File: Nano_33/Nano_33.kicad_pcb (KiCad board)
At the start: 2 copper layers, 2 parts, among them J1 Arduino-NANO-33

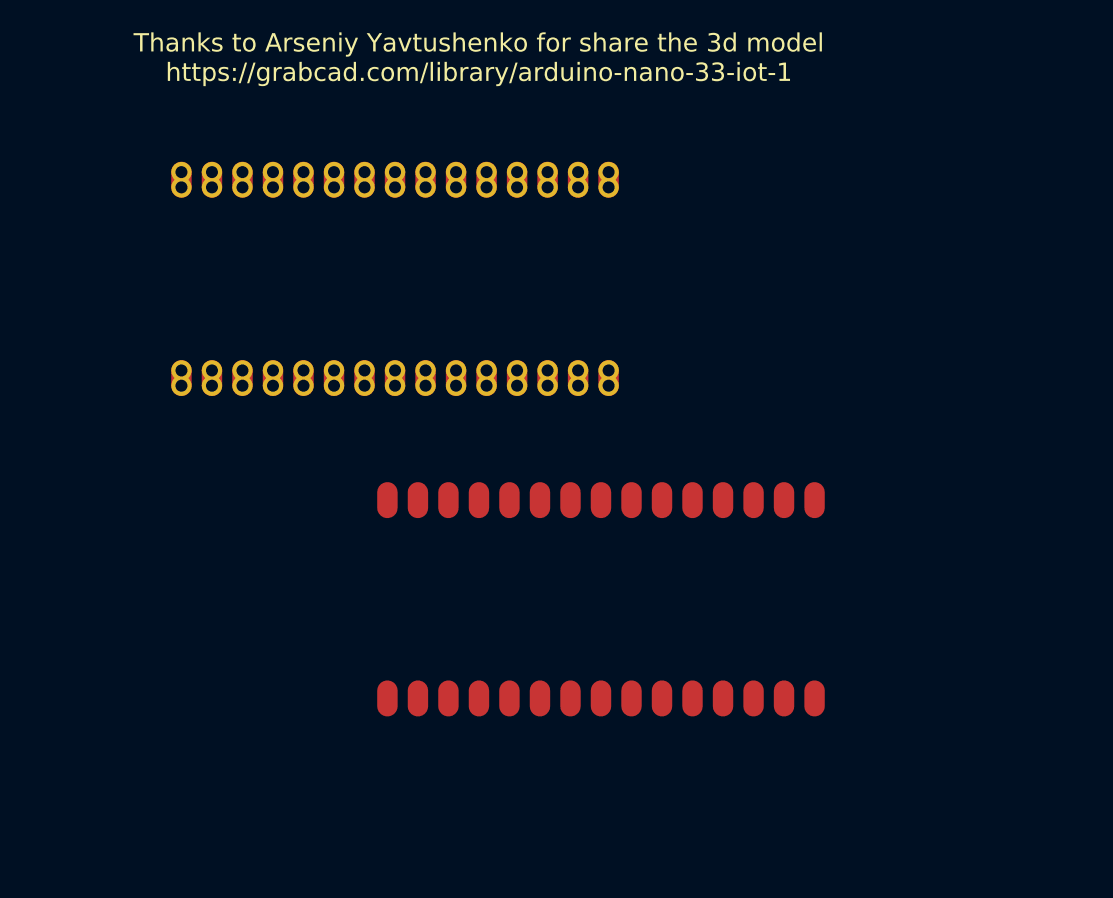
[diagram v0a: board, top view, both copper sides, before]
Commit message: Add No Castell Footprint
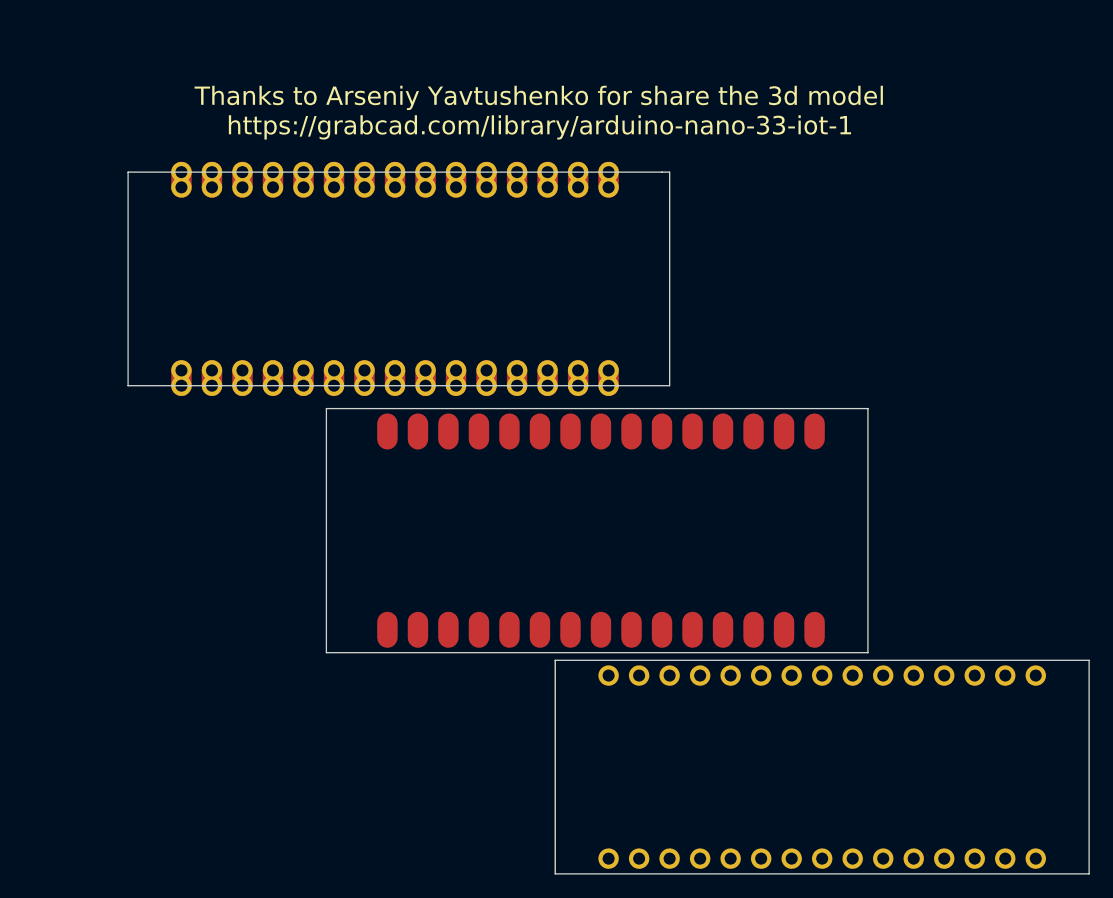
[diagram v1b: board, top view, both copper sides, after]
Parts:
- added REF**: NANO_33_Socket, Arduino:NANO_33_Socket, F.Cu at (186.1, 121.3)
- moved REF** 5.72 mm to (167.6, 101.6)
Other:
- board outline added: 80 x 58.4 mm
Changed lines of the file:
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@@
   (general
     (thickness 1.6002)
-    (drawings 1)
+    (drawings 14)
     (tracks 0)
     (zones 0)
-    (modules 2)
+    (modules 3)
     (nets 29)
   )
@@
     (add_net /VUSB)
   )
-  (module Arduino:NANO_33_Footprint_SMD_Castell (layer Front)
-    (at 167.64 107.315)
+  (module Arduino:NANO_33_Socket (layer Front)
+    (at 186.055 121.285)
     (descr "Through hole straight socket strip, 1x15, 2.54mm pitch")
     (tags "Through hole socket strip THT 1x15 2.54mm single row")
-    (fp_text reference REF** (at 0 -13.335) (layer F.Fab)
-      (effects (font (size 1 1) (thickness 0.15)))
-    )
-    (fp_text value NANO_33_Footprint_SMD_Castell (at 0 12.065) (layer F.Fab)
+    (fp_text reference REF** (at 20.32 -10.16) (layer F.Fab)
+      (effects (font (size 1 1) (thickness 0.15)))
+    )
+    (fp_text value NANO_33_Socket (at 0 12.065) (layer F.Fab)
+      (effects (font (size 1 1) (thickness 0.15)))
+    )
+    (fp_text user %R (at 0 -7.62) (layer F.Fab)
+      (effects (font (size 1 1) (thickness 0.15)))
+    )
+    (fp_line (start -19.05 -8.89) (end 19.05 -8.89) (layer F.Fab) (width 0.1))
+    (fp_line (start -19.05 -6.35) (end -19.05 -8.89) (layer F.Fab) (width 0.1))
+    (fp_line (start 18.415 -6.35) (end -19.05 -6.35) (layer F.Fab) (width 0.1))
+    (fp_line (start 19.05 -6.985) (end 18.415 -6.35) (layer F.Fab) (width 0.1))
+    (fp_line (start 19.05 -8.89) (end 19.05 -6.985) (layer F.Fab) (width 0.1))
+    (fp_line (start -19.05 8.89) (end -19.05 6.985) (layer F.Fab) (width 0.1))
+    (fp_line (start -19.05 6.985) (end -18.415 6.35) (layer F.Fab) (width 0.1))
+    (fp_line (start -18.415 6.35) (end 19.05 6.35) (layer F.Fab) (width 0.1))
+    (fp_line (start 19.05 6.35) (end 19.05 8.89) (layer F.Fab) (width 0.1))
+    (fp_line (start 19.05 8.89) (end -19.05 8.89) (layer F.Fab) (width 0.1))
+    (fp_text user %R (at 0 7.62 180) (layer F.Fab)
+      (effects (font (size 1 1) (thickness 0.15)))
+    )
+    (fp_line (start 22 8.89) (end 22 -8.89) (layer F.Fab) (width 0.12))
+    (fp_line (start -22 8.89) (end 22 8.89) (layer F.Fab) (width 0.12))
+    (fp_line (start -22 8.89) (end -22 -8.89) (layer F.Fab) (width 0.12))
+    (fp_line (start -22 -8.89) (end 22 -8.89) (layer F.Fab) (width 0.12))
+    (fp_poly (pts (xy -22.86 3.175) (xy -18.415 3.175) (xy -18.415 -3.175) (xy -22.86 -3.175)) (layer F.Fab) (width 0.1))
+    (fp_poly (pts (xy -3.175 3.175) (xy 3.175 3.175) (xy 3.175 -3.175) (xy -3.175 -3.175)) (layer F.Fab) (width 0.1))
+    (fp_poly (pts (xy 8.89 4.445) (xy 21.59 4.445) (xy 21.59 -4.445) (xy 8.89 -4.445)) (layer F.Fab) (width 0.1))
+    (pad 30 thru_hole oval (at -17.78 -7.62 270) (size 1.7 1.7) (drill 1) (layers *.Cu *.Mask))
+    (pad 29 thru_hole oval (at -15.24 -7.62 270) (size 1.7 1.7) (drill 1) (layers *.Cu *.Mask))
+    (pad 28 thru_hole oval (at -12.7 -7.62 270) (size 1.7 1.7) (drill 1) (layers *.Cu *.Mask))
+    (pad 27 thru_hole oval (at -10.16 -7.62 270) (size 1.7 1.7) (drill 1) (layers *.Cu *.Mask))
+    (pad 26 thru_hole oval (at -7.62 -7.62 270) (size 1.7 1.7) (drill 1) (layers *.Cu *.Mask))
+    (pad 25 thru_hole oval (at -5.08 -7.62 270) (size 1.7 1.7) (drill 1) (layers *.Cu *.Mask))
+    (pad 24 thru_hole oval (at -2.54 -7.62 270) (size 1.7 1.7) (drill 1) (layers *.Cu *.Mask))
+    (pad 23 thru_hole oval (at 0 -7.62 270) (size 1.7 1.7) (drill 1) (layers *.Cu *.Mask))
+    (pad 22 thru_hole oval (at 2.54 -7.62 270) (size 1.7 1.7) (drill 1) (layers *.Cu *.Mask))
+    (pad 21 thru_hole oval (at 5.08 -7.62 270) (size 1.7 1.7) (drill 1) (layers *.Cu *.Mask))
+    (pad 20 thru_hole oval (at 7.62 -7.62 270) (size 1.7 1.7) (drill 1) (layers *.Cu *.Mask))
+    (pad 19 thru_hole oval (at 10.16 -7.62 270) (size 1.7 1.7) (drill 1) (layers *.Cu *.Mask))
+    (pad 18 thru_hole oval (at 12.7 -7.62 270) (size 1.7 1.7) (drill 1) (layers *.Cu *.Mask))
+    (pad 17 thru_hole oval (at 15.24 -7.62 270) (size 1.7 1.7) (drill 1) (layers *.Cu *.Mask))
+    (pad 16 thru_hole circle (at 17.78 -7.62 270) (size 1.7 1.7) (drill 1) (layers *.Cu *.Mask))
+    (pad 12 thru_hole oval (at 10.16 7.62 90) (size 1.7 1.7) (drill 1) (layers *.Cu *.Mask))
+    (pad 15 thru_hole oval (at 17.78 7.62 90) (size 1.7 1.7) (drill 1) (layers *.Cu *.Mask))
+    (pad 1 thru_hole circle (at -17.78 7.62 90) (size 1.7 1.7) (drill 1) (layers *.Cu *.Mask))
+    (pad 2 thru_hole oval (at -15.24 7.62 90) (size 1.7 1.7) (drill 1) (layers *.Cu *.Mask))
+    (pad 3 thru_hole oval (at -12.7 7.62 90) (size 1.7 1.7) (drill 1) (layers *.Cu *.Mask))
+    (pad 4 thru_hole oval (at -10.16 7.62 90) (size 1.7 1.7) (drill 1) (layers *.Cu *.Mask))
+    (pad 5 thru_hole oval (at -7.62 7.62 90) (size 1.7 1.7) (drill 1) (layers *.Cu *.Mask))
+    (pad 14 thru_hole oval (at 15.24 7.62 90) (size 1.7 1.7) (drill 1) (layers *.Cu *.Mask))
+    (pad 6 thru_hole oval (at -5.08 7.62 90) (size 1.7 1.7) (drill 1) (layers *.Cu *.Mask))
+    (pad 11 thru_hole oval (at 7.62 7.62 90) (size 1.7 1.7) (drill 1) (layers *.Cu *.Mask))
+    (pad 10 thru_hole oval (at 5.08 7.62 90) (size 1.7 1.7) (drill 1) (layers *.Cu *.Mask))
+    (pad 7 thru_hole oval (at -2.54 7.62 90) (size 1.7 1.7) (drill 1) (layers *.Cu *.Mask))
+    (pad 8 thru_hole oval (at 0 7.62 90) (size 1.7 1.7) (drill 1) (layers *.Cu *.Mask))
+    (pad 9 thru_hole oval (at 2.54 7.62 90) (size 1.7 1.7) (drill 1) (layers *.Cu *.Mask))
+    (pad 13 thru_hole oval (at 12.7 7.62 90) (size 1.7 1.7) (drill 1) (layers *.Cu *.Mask))
+    (model "${KISYS3DMOD}/Arduino.3dshapes/Arduino Nano 33 IoT.stp"
+      (offset (xyz 0.5 0 4))
+      (scale (xyz 1 1 1))
+      (rotate (xyz -90 0 90))
+    )
+    (model ${KISYS3DMOD}/Connector_PinHeader_2.54mm.3dshapes/PinHeader_1x15_P2.54mm_Vertical.wrl
+      (offset (xyz 17.8 -7.6 3))
+      (scale (xyz 1 1 1))
+      (rotate (xyz 0 180 90))
+    )
+    (model ${KISYS3DMOD}/Connector_PinHeader_2.54mm.3dshapes/PinHeader_1x15_P2.54mm_Vertical.wrl
+      (offset (xyz 17.8 7.6 3))
+      (scale (xyz 1 1 1))
+      (rotate (xyz 0 180 90))
+    )
+  )
+  (module Arduino:NANO_33_Footprint_SMD_Castell (layer Front)
+    (at 167.64 101.6)
+    (descr "Through hole straight socket strip, 1x15, 2.54mm pitch")
+    (tags "Through hole socket strip THT 1x15 2.54mm single row")
+    (fp_text reference REF** (at 19.05 -11.43) (layer F.Fab)
+      (effects (font (size 1 1) (thickness 0.15)))
+    )
+    (fp_text value NANO_33_Footprint_SMD_Castell (at -19.05 11.43) (layer F.Fab)
       (effects (font (size 1 1) (thickness 0.15)))
     )
@@
     (descr "Through hole straight socket strip, 1x15, 2.54mm pitch")
     (tags "Through hole socket strip THT 1x15 2.54mm single row")
-    (fp_text reference J1 (at 0 -13.335) (layer F.Fab)
-      (effects (font (size 1 1) (thickness 0.15)))
-    )
-    (fp_text value Arduino-NANO-33 (at 0 12.065) (layer F.Fab)
+    (fp_text reference J1 (at -24.13 -9.525) (layer F.Fab)
+      (effects (font (size 1 1) (thickness 0.15)))
+    )
+    (fp_text value Arduino-NANO-33 (at -13.97 11.43) (layer F.Fab)
       (effects (font (size 1 1) (thickness 0.15)))
     )
@@
     )
   )
-  (gr_text "Thanks to Arseniy Yavtushenko for share the 3d model \nhttps://grabcad.com/library/arduino-nano-33-iot-1" (at 157.48 62.23) (layer F.SilkS)
+  (gr_line (start 208.28 130.175) (end 208.28 112.395) (layer Edge.Cuts) (width 0.0381))
+  (gr_line (start 163.83 130.175) (end 208.28 130.175) (layer Edge.Cuts) (width 0.0381))
+  (gr_line (start 163.83 112.395) (end 163.83 130.175) (layer Edge.Cuts) (width 0.0381))
+  (gr_line (start 208.28 112.395) (end 163.83 112.395) (layer Edge.Cuts) (width 0.0381))
+  (gr_line (start 189.865 111.76) (end 189.865 91.44) (layer Edge.Cuts) (width 0.0381))
+  (gr_line (start 144.78 111.76) (end 189.865 111.76) (layer Edge.Cuts) (width 0.0381))
+  (gr_line (start 144.78 91.44) (end 144.78 111.76) (layer Edge.Cuts) (width 0.0381))
+  (gr_line (start 189.865 91.44) (end 144.78 91.44) (layer Edge.Cuts) (width 0.0381))
+  (gr_line (start 173.355 71.755) (end 173.355 89.535) (layer Edge.Cuts) (width 0.0381))
+  (gr_line (start 172.72 71.755) (end 173.355 71.755) (layer Edge.Cuts) (width 0.0381))
+  (gr_line (start 128.27 71.755) (end 172.72 71.755) (layer Edge.Cuts) (width 0.0381))
+  (gr_line (start 128.27 89.535) (end 128.27 71.755) (layer Edge.Cuts) (width 0.0381))
+  (gr_line (start 173.355 89.535) (end 128.27 89.535) (layer Edge.Cuts) (width 0.0381))
+  (gr_text "Thanks to Arseniy Yavtushenko for share the 3d model \nhttps://grabcad.com/library/arduino-nano-33-iot-1" (at 162.56 66.675) (layer F.SilkS)
     (effects (font (size 1.524 1.524) (thickness 0.3048)))
   )
